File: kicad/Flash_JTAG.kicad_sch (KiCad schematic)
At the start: 56 parts, among them J1 USB Type C, Q1 MMST2222A, SW1 User, U1 LFE5U-25F-6BG381C, U2 IS25LP128F, U3 FT231XQ, Y1 50MHz

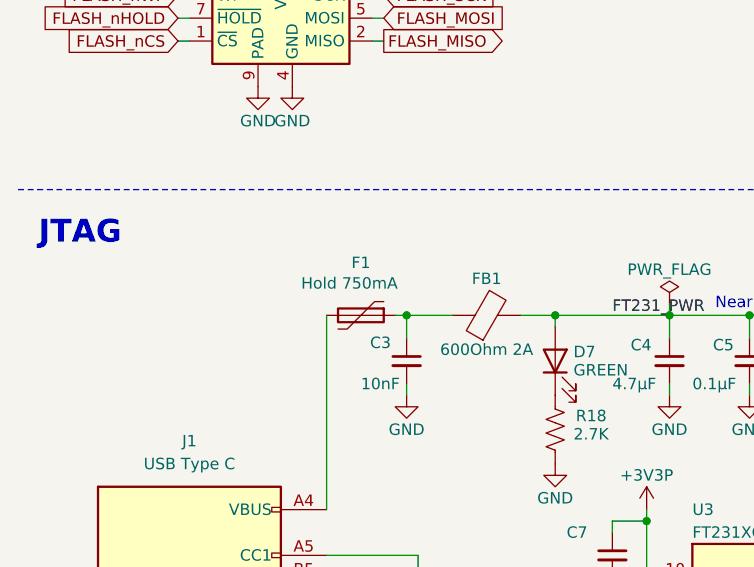
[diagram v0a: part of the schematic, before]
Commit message: Changed the FT231X fuse
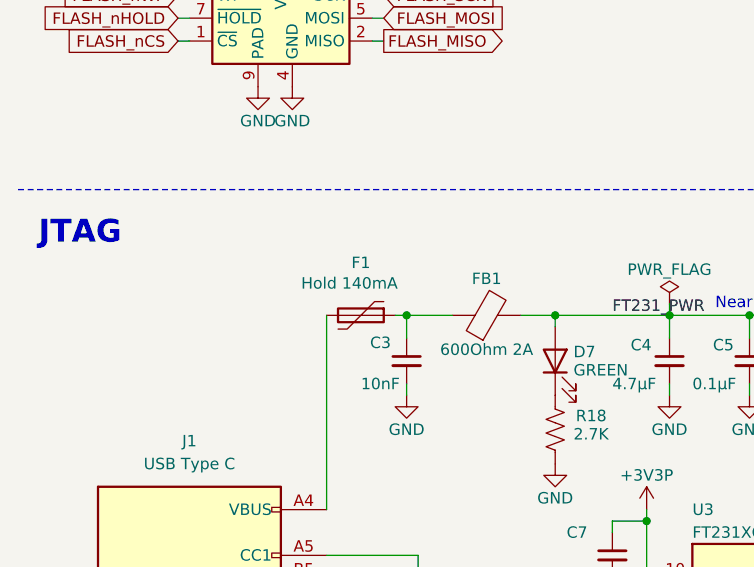
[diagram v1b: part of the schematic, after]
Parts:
- F1: value Hold 750mA -> Hold 140mA; MPN 0ZCG0075FF2C -> 0ZCG0014FF2C
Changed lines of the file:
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@@
 			)
 		)
-		(property "Value" "Hold 750mA"
+		(property "Value" "Hold 140mA"
 			(at 49.53 100.584 90)
 			(effects
@@
 			)
 		)
-		(property "Description" "PTC RESET FUSE 16V 750MA 1812"
+		(property "Description" "PTC RESET FUSE 60V 140MA 1812"
 			(at 50.8 104.14 0)
 			(effects
@@
 			)
 		)
-		(property "MPN" "0ZCG0075FF2C"
+		(property "MPN" "0ZCG0014FF2C"
 			(at 50.8 104.14 0)
 			(effects
